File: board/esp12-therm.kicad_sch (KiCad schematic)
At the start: 21 parts, among them J1 BATT, J2 I2C, J4 1W, Q1 IRLML6401, U1 TP4056_board, U2 ESP-12E

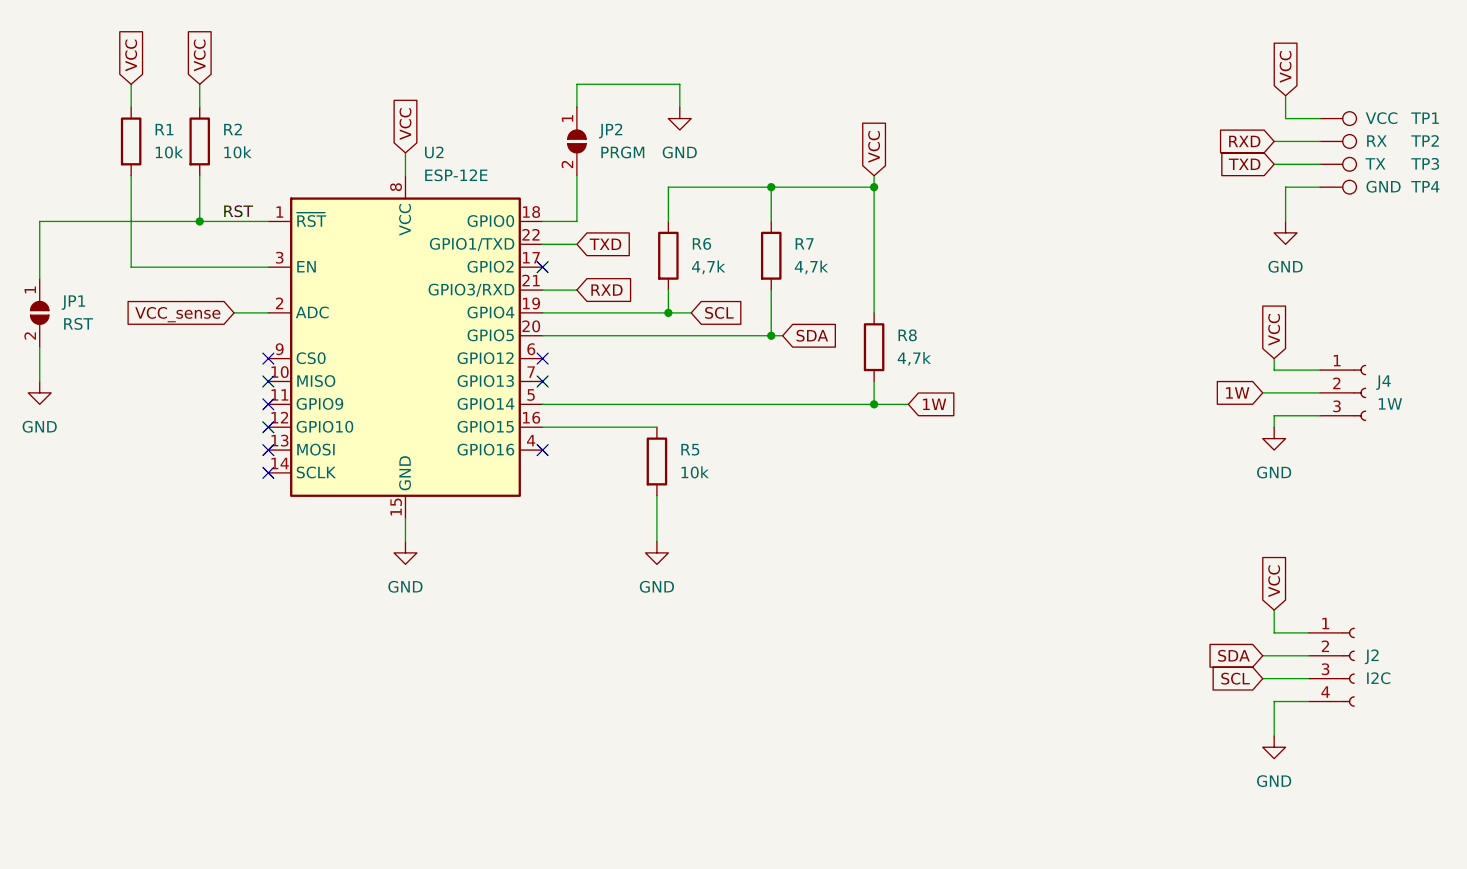
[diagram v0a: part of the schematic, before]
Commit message: Add JLC labels and silkscreen update, make board round
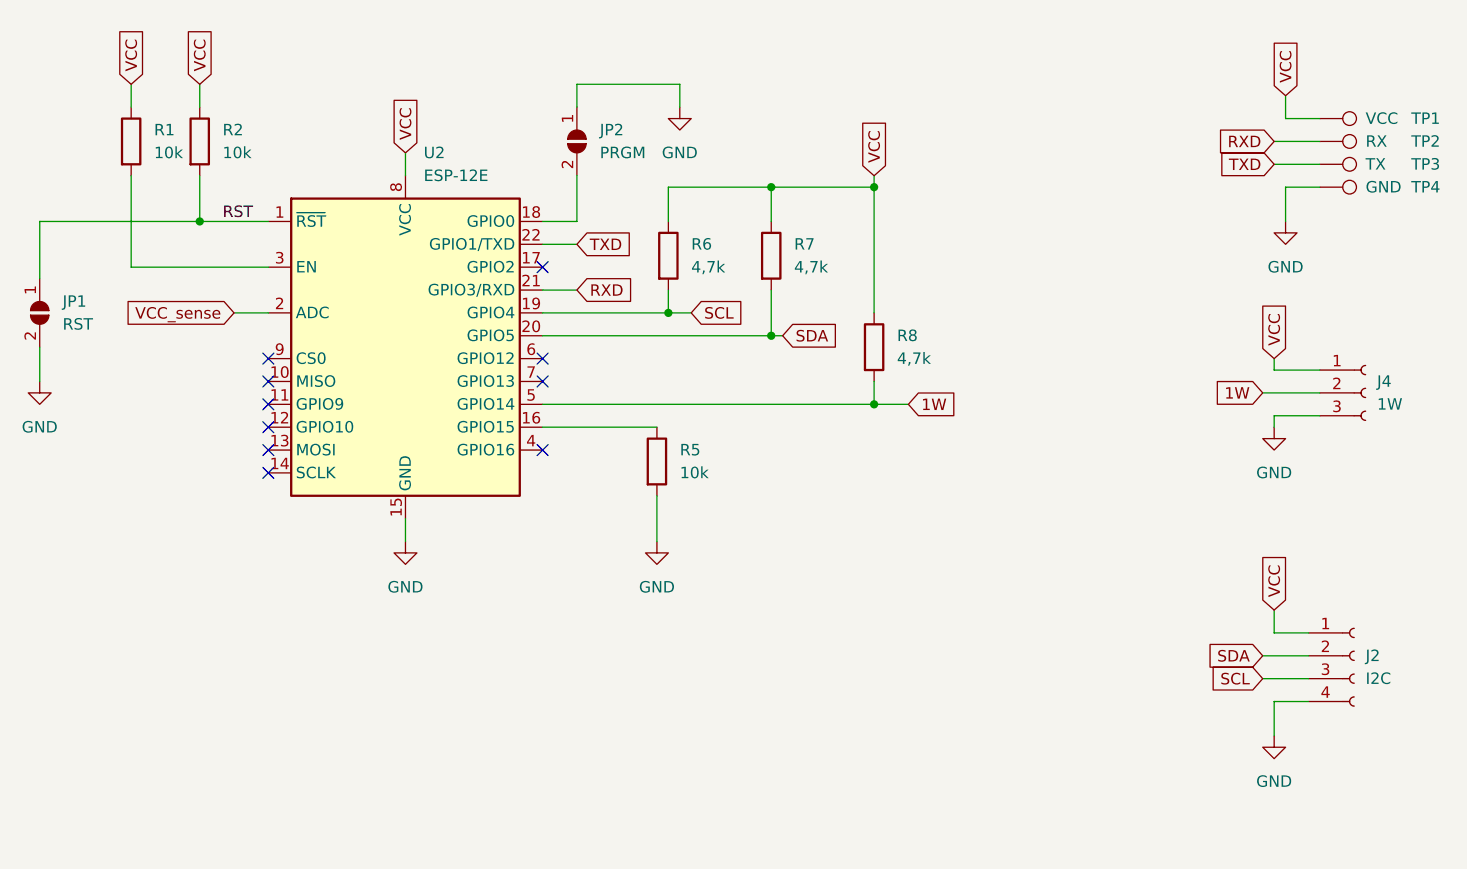
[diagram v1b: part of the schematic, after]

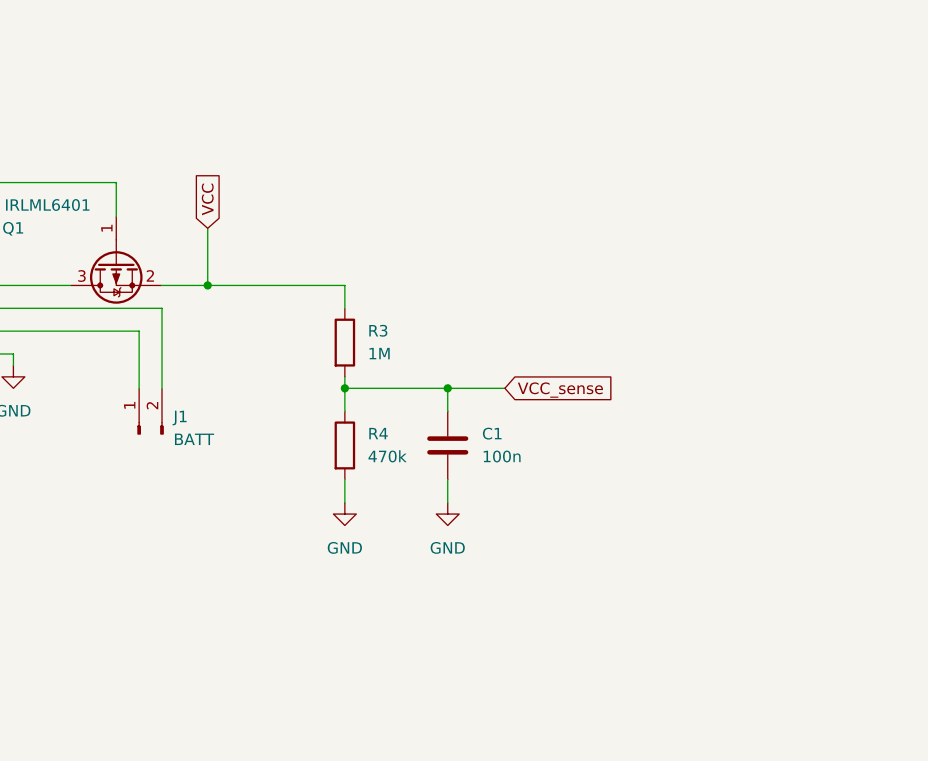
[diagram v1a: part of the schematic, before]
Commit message: Add Voltage regulator to board
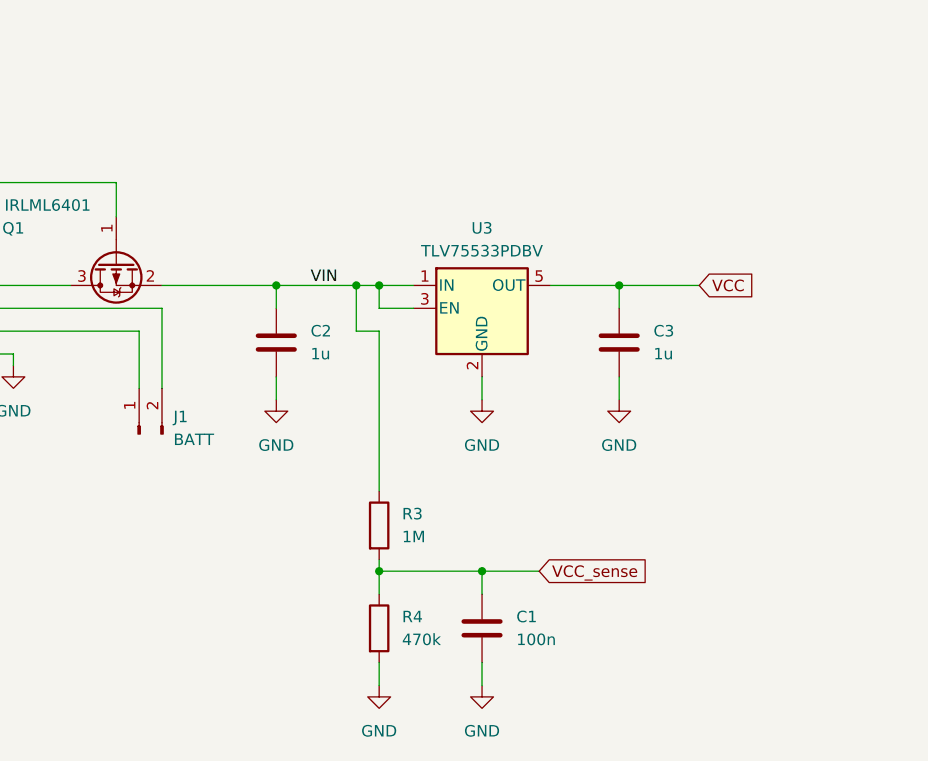
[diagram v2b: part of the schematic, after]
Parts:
- added C2, C3: 1u, Capacitor_SMD:C_0805_2012Metric_Pad1.18x1.45mm_HandSolder, symbol Device:C
- added U3: TLV75533PDBV, Package_TO_SOT_SMD:SOT-23-5, symbol Regulator_Linear:TLV75533PDBV
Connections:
- net GND: now also C2.2, C3.2, U3.2 (GND)
- net VCC: now also C3.1, U3.5 (OUT); no longer Q1.2 (S), R3.1
- new net VIN: C2.1, Q1.2 (S), R3.1, U3.1 (IN), U3.3 (EN)
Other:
- moved on the sheet: C1, R3, R4

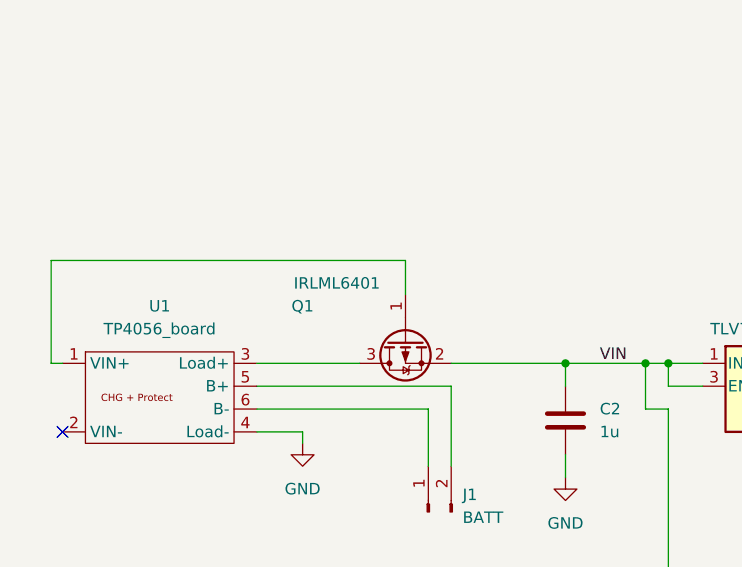
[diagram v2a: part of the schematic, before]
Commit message: Change input MOSFET to an available one
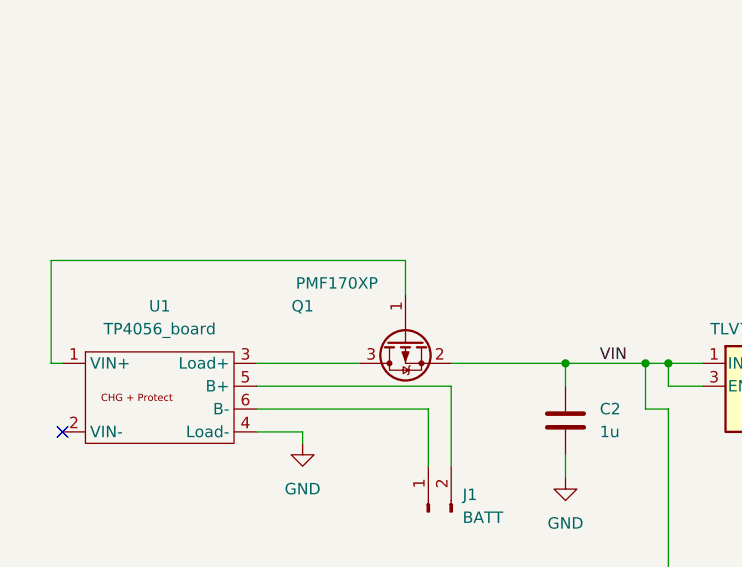
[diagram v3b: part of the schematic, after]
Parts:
- Q1: value IRLML6401 -> PMF170XP; footprint Package_TO_SOT_SMD:SOT-23 -> Package_TO_SOT_SMD:SOT-23-3
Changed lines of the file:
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@@
       (effects (font (size 1.27 1.27)))
     )
-    (property "Value" "IRLML6401" (at 58.42 118.11 90)
+    (property "Value" "PMF170XP" (at 58.42 118.11 90)
       (effects (font (size 1.27 1.27)))
     )
-    (property "Footprint" "Package_TO_SOT_SMD:SOT-23" (at 67.945 129.54 0)
+    (property "Footprint" "Package_TO_SOT_SMD:SOT-23-3" (at 67.945 129.54 0)
       (effects (font (size 1.27 1.27) italic) (justify left) hide)
     )

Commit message: * Adapt footprints to new MOSFET * Place battery bypass solder jumper
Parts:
- added JP3: no battery bridge, Jumper:SolderJumper-2_P1.3mm_Open_RoundedPad1.0x1.5mm, symbol Jumper:SolderJumper_2_Open
- Q1: footprint Package_TO_SOT_SMD:SOT-23-3 -> Package_TO_SOT_SMD:SOT-323_SC-70_Handsoldering
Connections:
- net GND: now also U1.2 (VIN-)
- net VIN: now also JP3.2 (B)
- net at Q1.1 (G), U1.1 (VIN+): now also JP3.1 (A)
- no-connect marks 11 -> 10
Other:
- note added: "This PMOS disconnects the whole circuit while the battery is charged. This means you cannot use it while charging. If you don't use this circuit with a battery or the charging circuit, bridge JP3 and connect the power supply to VIN+ and VIN-"
- moved on the sheet: J1, R3
